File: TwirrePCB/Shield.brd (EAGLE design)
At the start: 96.2 x 53.6 mm, 60 parts, among them Q1 BSS138, Q2 BSS138, T2 BC847, U1 ARDUINO-MEGAPRO

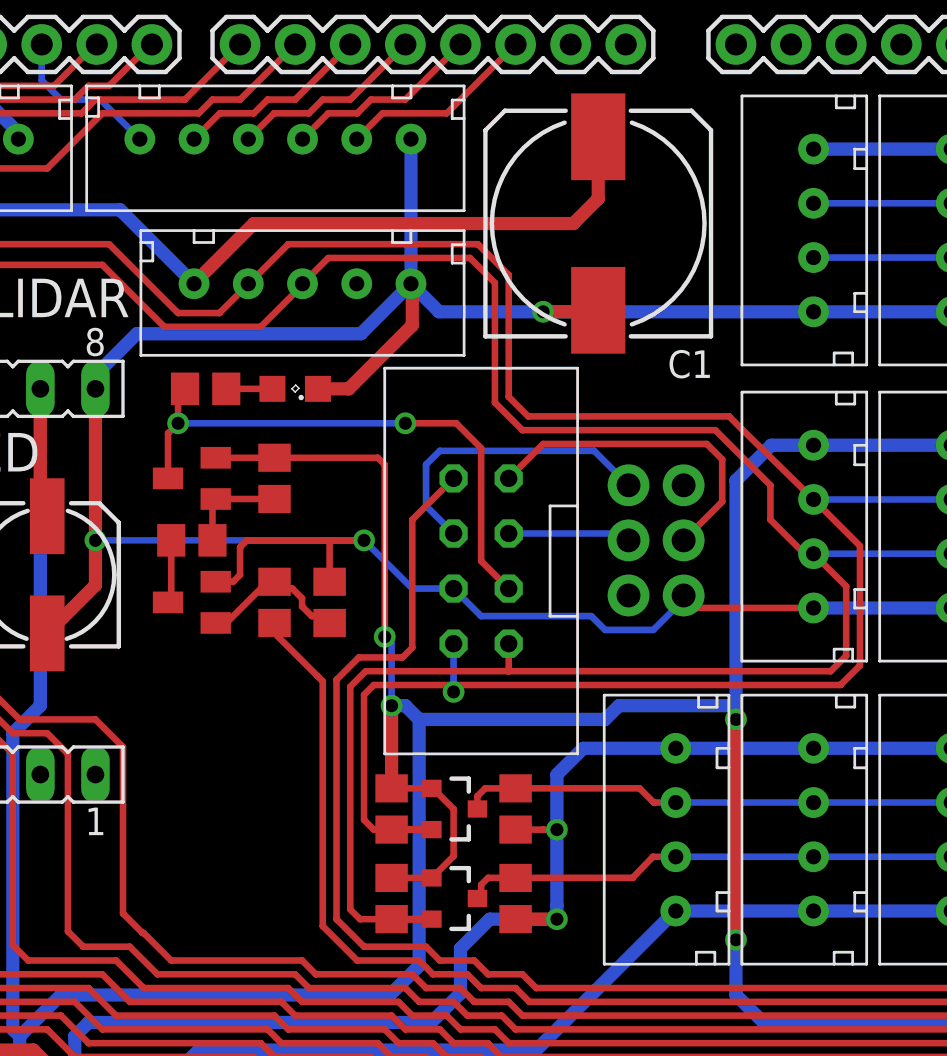
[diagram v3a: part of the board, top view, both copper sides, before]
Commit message: Minor trace modifications
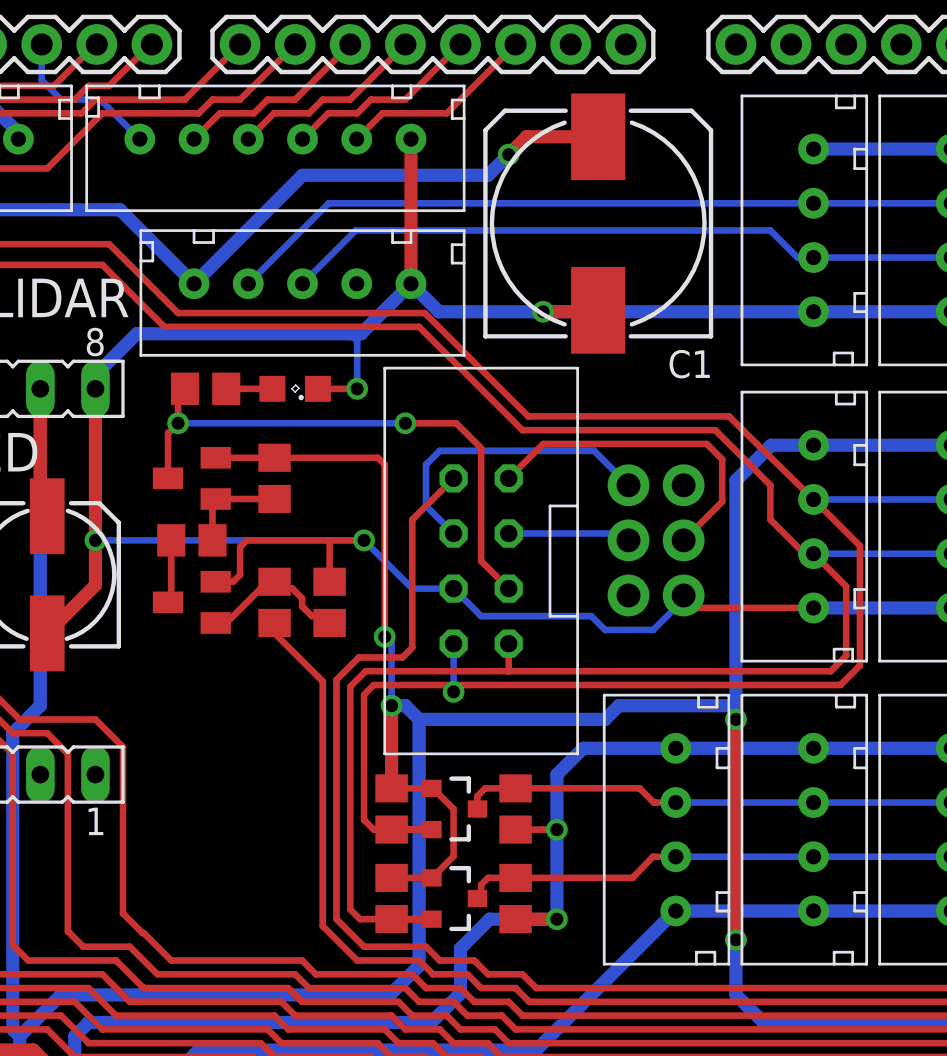
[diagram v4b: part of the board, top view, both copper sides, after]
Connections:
- net SCL_HS: now also U$12.3
- net SCL_LS: no longer U$12.3
- net SDA_HS: now also U$12.4
- net SDA_LS: no longer U$12.4
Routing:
- net SDA_HS: track 21.7 -> 49.3 mm
- net SCL_HS: track 23.7 -> 48.8 mm
- net SDA_LS: track 131.4 -> 125.5 mm
- net SCL_LS: track 135.1 -> 129.2 mm
- net GND: track 433.0 -> 430.0 mm, vias 7 -> 8
- net +5V: track 252.2 -> 250.5 mm, vias 5 -> 6
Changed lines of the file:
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@@
 <wire x1="43.46" y1="38.4775" x2="48.26" y2="38.4775" width="0.6096" layer="16"/>
 <wire x1="48.26" y1="38.4775" x2="60.725" y2="38.4775" width="0.6096" layer="16"/>
-<wire x1="37.88" y1="34.925" x2="39.300296875" y2="34.925" width="0.6096" layer="1"/>
-<wire x1="39.300296875" y1="34.925" x2="42.2275" y2="37.852203125" width="0.6096" layer="1"/>
-<wire x1="42.2275" y1="37.852203125" x2="42.2275" y2="39.4525" width="0.6096" layer="1"/>
 <contactref element="U$13" pad="1"/>
 <wire x1="1.533025" y1="21.59" x2="1.533025" y2="21.65" width="0.6096" layer="16"/>
@@
 <wire x1="17.145" y1="22.86" x2="15.875" y2="21.65" width="0.3048" layer="16"/>
 <wire x1="15.875" y1="21.65" x2="3.2575" y2="21.65" width="0.3048" layer="16"/>
-<wire x1="42.2275" y1="39.4525" x2="42.1675" y2="39.77" width="0.6096" layer="1"/>
 <contactref element="SV2" pad="8"/>
 <wire x1="27.6225" y1="34.925" x2="27.6225" y2="35.56" width="0.6096" layer="16"/>
 <wire x1="27.6225" y1="35.56" x2="29.5275" y2="37.465" width="0.6096" layer="16"/>
-<wire x1="29.5275" y1="37.465" x2="39.8625" y2="37.465" width="0.6096" layer="16"/>
+<wire x1="29.5275" y1="37.465" x2="39.37" y2="37.465" width="0.6096" layer="16"/>
+<wire x1="39.37" y1="37.465" x2="39.8625" y2="37.465" width="0.6096" layer="16"/>
 <wire x1="39.8625" y1="37.465" x2="42.1675" y2="39.77" width="0.6096" layer="16"/>
 <contactref element="U$14" pad="1"/>
@@
 <wire x1="14.986" y1="50.8" x2="14.986" y2="48.514" width="0.6096" layer="16"/>
 <wire x1="14.986" y1="48.514" x2="15.24" y2="48.26" width="0.6096" layer="16"/>
-<wire x1="42.1675" y1="39.77" x2="42.1675" y2="46.4375" width="0.6096" layer="16"/>
 <contactref element="U$25" pad="5"/>
 <wire x1="44.1325" y1="25.7175" x2="42.2275" y2="25.7175" width="0.3048" layer="16"/>
@@
 <vertex x="-1.27" y="13.0175"/>
 </polygon>
+<wire x1="37.88" y1="34.925" x2="39.6875" y2="34.925" width="0.3048" layer="1"/>
+<via x="39.6875" y="34.925" extent="1-16" drill="0.6" shape="square"/>
+<wire x1="39.6875" y1="34.925" x2="39.6875" y2="37.1475" width="0.3048" layer="16"/>
+<wire x1="39.6875" y1="37.1475" x2="39.37" y2="37.465" width="0.3048" layer="16"/>
+<wire x1="6.0325" y1="6.81" x2="6.35" y2="11.1125" width="0" layer="19" extent="16-16"/>
+<wire x1="42.1675" y1="46.4375" x2="42.1675" y2="39.77" width="0.6096" layer="1"/>
 </signal>
 <signal name="SPI_VIN">
@@
 <wire x1="62.23" y1="22.61745" x2="62.23" y2="25.82" width="0.3048" layer="1"/>
 <wire x1="62.23" y1="25.82" x2="60.725" y2="27.325" width="0.3048" layer="1"/>
-<contactref element="U$12" pad="3"/>
 <wire x1="16.8275" y1="40.64" x2="20.0025" y2="40.64" width="0.3048" layer="1"/>
 <wire x1="20.0025" y1="40.64" x2="27.94" y2="40.64" width="0.3048" layer="1"/>
 <wire x1="27.94" y1="40.64" x2="30.7975" y2="37.7825" width="0.3048" layer="1"/>
-<wire x1="30.7975" y1="37.7825" x2="35.2425" y2="37.7825" width="0.3048" layer="1"/>
-<wire x1="35.2425" y1="37.7825" x2="37.1675" y2="39.7075" width="0.3048" layer="1"/>
-<wire x1="37.1675" y1="39.7075" x2="37.1675" y2="39.77" width="0.3048" layer="1"/>
-<wire x1="37.1675" y1="39.77" x2="38.355" y2="40.9575" width="0.3048" layer="1"/>
 <contactref element="SV2" pad="5"/>
 <wire x1="20.0025" y1="34.925" x2="20.0025" y2="40.64" width="0.3048" layer="1"/>
-<wire x1="38.355" y1="40.9575" x2="44.8927375" y2="40.9575" width="0.3048" layer="1"/>
-<wire x1="44.8927375" y1="40.9575" x2="46.0375" y2="39.8127375" width="0.3048" layer="1"/>
 <wire x1="16.8275" y1="40.64" x2="7.3025" y2="50.165" width="0.3048" layer="1"/>
 <wire x1="7.3025" y1="50.165" x2="7.3025" y2="50.7365" width="0.3048" layer="1"/>
@@
 <wire x1="58.7375" y1="30.48" x2="56.1975" y2="33.02" width="0.3048" layer="1"/>
 <wire x1="56.1975" y1="33.02" x2="47.3075" y2="33.02" width="0.3048" layer="1"/>
-<wire x1="47.3075" y1="33.02" x2="46.0375" y2="34.29" width="0.3048" layer="1"/>
-<wire x1="46.0375" y1="34.29" x2="46.0375" y2="39.8127375" width="0.3048" layer="1"/>
+<wire x1="30.7975" y1="37.7825" x2="42.545" y2="37.7825" width="0.3048" layer="1"/>
+<wire x1="42.545" y1="37.7825" x2="47.3075" y2="33.02" width="0.3048" layer="1"/>
 </signal>
 <signal name="SDA_LS">
@@
 <wire x1="60.725" y1="29.825" x2="67.075" y2="29.825" width="0.3048" layer="16"/>
 <wire x1="56.8325" y1="33.655" x2="47.570525" y2="33.655" width="0.3048" layer="1"/>
-<wire x1="47.570525" y1="33.655" x2="46.6725" y2="34.553025" width="0.3048" layer="1"/>
-<wire x1="46.6725" y1="34.553025" x2="46.6725" y2="40.172596875" width="0.3048" layer="1"/>
 <wire x1="56.8325" y1="33.655" x2="57.4675" y2="33.02" width="0.3048" layer="1"/>
 <wire x1="57.4675" y1="33.02" x2="60.725" y2="29.825" width="0.3048" layer="1"/>
@@
 <wire x1="62.865" y1="22.170525" x2="62.865" y2="27.685" width="0.3048" layer="1"/>
 <wire x1="62.865" y1="27.685" x2="60.725" y2="29.825" width="0.3048" layer="1"/>
-<contactref element="U$12" pad="4"/>
 <wire x1="17.145" y1="41.5925" x2="22.5425" y2="41.5925" width="0.3048" layer="1"/>
 <wire x1="22.5425" y1="41.5925" x2="28.2575" y2="41.5925" width="0.3048" layer="1"/>
 <wire x1="28.2575" y1="41.5925" x2="31.4325" y2="38.4175" width="0.3048" layer="1"/>
-<wire x1="31.4325" y1="38.4175" x2="33.3375" y2="38.4175" width="0.3048" layer="1"/>
-<wire x1="33.3375" y1="38.4175" x2="34.6675" y2="39.7475" width="0.3048" layer="1"/>
-<wire x1="34.6675" y1="39.7475" x2="34.6675" y2="39.77" width="0.3048" layer="1"/>
-<wire x1="34.6675" y1="39.7475" x2="36.5125" y2="41.5925" width="0.3048" layer="1"/>
 <contactref element="SV2" pad="6"/>
 <wire x1="22.5425" y1="34.925" x2="22.5425" y2="41.5925" width="0.3048" layer="16"/>
 <via x="22.5425" y="41.5925" extent="1-16" drill="0.6" shape="square"/>
-<wire x1="46.6725" y1="40.172596875" x2="45.252596875" y2="41.5925" width="0.3048" layer="1"/>
-<wire x1="45.252596875" y1="41.5925" x2="36.5125" y2="41.5925" width="0.3048" layer="1"/>
 <wire x1="17.145" y1="41.5925" x2="9.8425" y2="48.895" width="0.3048" layer="1"/>
 <wire x1="9.8425" y1="48.895" x2="9.8425" y2="50.7365" width="0.3048" layer="1"/>
@@
 <via x="44.1325" y="20.955" extent="1-16" drill="0.6" shape="square"/>
 <wire x1="44.1325" y1="20.955" x2="44.1325" y2="21.2725" width="0.3048" layer="1"/>
+<wire x1="31.4325" y1="38.4175" x2="42.808025" y2="38.4175" width="0.3048" layer="1"/>
+<wire x1="42.808025" y1="38.4175" x2="47.570525" y2="33.655" width="0.3048" layer="1"/>
 </signal>
 <signal name="+5V">
@@
 <wire x1="90.805" y1="47.625" x2="90.4875" y2="47.3075" width="0.4064" layer="16"/>
 <contactref element="C1" pad="+"/>
-<wire x1="50.8" y1="46.545" x2="50.8" y2="43.6897625" width="0.6096" layer="1"/>
-<wire x1="50.8" y1="43.6897625" x2="49.6552375" y2="42.545" width="0.6096" layer="1"/>
-<wire x1="49.6552375" y1="42.545" x2="34.925" y2="42.545" width="0.6096" layer="1"/>
-<wire x1="34.925" y1="42.545" x2="32.1675" y2="39.7875" width="0.6096" layer="1"/>
-<wire x1="32.1675" y1="39.7875" x2="32.1675" y2="39.77" width="0.6096" layer="1"/>
 <wire x1="54.375" y1="18.355" x2="50.105" y2="18.355" width="0.6096" layer="16"/>
 <wire x1="50.105" y1="18.355" x2="48.895" y2="17.145" width="0.6096" layer="16"/>
 <wire x1="48.895" y1="17.145" x2="48.895" y2="14.605" width="0.6096" layer="16"/>
 <wire x1="45.7970375" y1="10.4775" x2="48.895" y2="10.4775" width="0.6096" layer="16"/>
-<wire x1="48.895" y1="11.1125" x2="48.895" y2="14.605" width="0.6096" layer="16"/>
+<wire x1="48.895" y1="10.4775" x2="48.895" y2="14.605" width="0.6096" layer="16"/>
 <wire x1="46.99" y1="10.48" x2="48.8925" y2="10.48" width="0.6096" layer="1"/>
 <wire x1="48.8925" y1="10.48" x2="48.895" y2="10.4775" width="0.6096" layer="1"/>
 <via x="48.895" y="10.4775" extent="1-16" drill="0.6" shape="square"/>
-<wire x1="48.895" y1="10.4775" x2="48.895" y2="11.1125" width="0.6096" layer="16"/>
+<wire x1="50.8" y1="46.545" x2="47.4975" y2="46.545" width="0.6096" layer="1"/>
+<wire x1="47.4975" y1="46.545" x2="46.6725" y2="45.72" width="0.6096" layer="1"/>
+<via x="46.6725" y="45.72" extent="1-16" drill="0.6" shape="square"/>
+<wire x1="46.6725" y1="45.72" x2="45.72" y2="44.7675" width="0.6096" layer="16"/>
+<wire x1="45.72" y1="44.7675" x2="37.165" y2="44.7675" width="0.6096" layer="16"/>
+<wire x1="37.165" y1="44.7675" x2="32.1675" y2="39.77" width="0.6096" layer="16"/>
 </signal>
 <signal name="SDA_LS_5">
@@
 <wire x1="73.9775" y1="47.3075" x2="73.9775" y2="49.2125" width="0.3048" layer="16"/>
 <wire x1="73.9775" y1="49.2125" x2="72.39" y2="50.8" width="0.3048" layer="16"/>
+<contactref element="U$12" pad="4"/>
+<wire x1="60.725" y1="43.4775" x2="38.375" y2="43.4775" width="0.3048" layer="16"/>
+<wire x1="38.375" y1="43.4775" x2="34.6675" y2="39.77" width="0.3048" layer="16"/>
 </signal>
 <signal name="SCL_HS">
@@
 <wire x1="75.565" y1="46.6725" x2="74.93" y2="47.3075" width="0.3048" layer="16"/>
 <wire x1="74.93" y1="47.3075" x2="74.93" y2="50.8" width="0.3048" layer="16"/>
+<contactref element="U$12" pad="3"/>
+<wire x1="60.725" y1="40.9775" x2="59.9875" y2="40.9775" width="0.3048" layer="16"/>
+<wire x1="59.9875" y1="40.9775" x2="58.7375" y2="42.2275" width="0.3048" layer="16"/>
+<wire x1="58.7375" y1="42.2275" x2="39.625" y2="42.2275" width="0.3048" layer="16"/>
+<wire x1="39.625" y1="42.2275" x2="37.1675" y2="39.77" width="0.3048" layer="16"/>
 </signal>
 <signal name="N$7">

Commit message: Increase LED Resistor values
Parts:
- R20, R21, R6, R7: value 100 -> 220
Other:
- board text added: "FLIR"
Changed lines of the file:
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@@
 <grid distance="0.0125" unitdist="inch" unit="inch" style="lines" multiple="1" display="no" altdistance="0.025" altunitdist="inch" altunit="inch"/>
 <layers>
-<layer number="1" name="Top" color="4" fill="1" visible="yes" active="yes"/>
-<layer number="16" name="Bottom" color="1" fill="1" visible="yes" active="yes"/>
+<layer number="1" name="Top" color="4" fill="1" visible="no" active="yes"/>
+<layer number="16" name="Bottom" color="1" fill="1" visible="no" active="yes"/>
 <layer number="17" name="Pads" color="2" fill="1" visible="yes" active="yes"/>
 <layer number="18" name="Vias" color="2" fill="1" visible="yes" active="yes"/>
@@
 <dimension x1="-1.27" y1="53.33" x2="94.92" y2="53.33" x3="46.825" y3="59.3725" textsize="1.778" layer="37"/>
 <dimension x1="94.92" y1="53.33" x2="94.92" y2="-0.3175" x3="100.6475" y3="26.50625" textsize="1.778" layer="37"/>
+<text x="34.29" y="19.05" size="1.9304" layer="25">FLIR</text>
 </plain>
 <attributes>
@@
 <attribute name="VALUE" x="14.605" y="33.02" size="1.27" layer="27" rot="R180"/>
 </element>
-<element name="R20" library="resistor" package="R0805" value="100" x="8.89" y="42.2275" smashed="yes">
+<element name="R20" library="resistor" package="R0805" value="220" x="8.89" y="42.2275" smashed="yes">
 <attribute name="VALUE" x="8.255" y="39.6875" size="1.27" layer="27"/>
 </element>
-<element name="R6" library="resistor" package="R0805" value="100" x="8.89" y="40.005" smashed="yes">
+<element name="R6" library="resistor" package="R0805" value="220" x="8.89" y="40.005" smashed="yes">
 <attribute name="VALUE" x="8.255" y="37.465" size="1.27" layer="27"/>
 </element>
-<element name="R7" library="resistor" package="R0805" value="100" x="8.89" y="37.7825" smashed="yes">
+<element name="R7" library="resistor" package="R0805" value="220" x="8.89" y="37.7825" smashed="yes">
 <attribute name="VALUE" x="8.255" y="35.2425" size="1.27" layer="27"/>
 </element>
@@
 <element name="U$14" library="Arduino-Boards" package="JST-3" value="JST-3" x="89.8525" y="22.5425" rot="R90"/>
 <element name="U$15" library="Arduino-Boards" package="JST-3" value="JST-3" x="89.8525" y="12.065" rot="R90"/>
-<element name="R21" library="resistor" package="R0805" value="100" x="89.8525" y="51.1175" smashed="yes">
+<element name="R21" library="resistor" package="R0805" value="220" x="89.8525" y="51.1175" smashed="yes">
 <attribute name="VALUE" x="89.2175" y="48.5775" size="1.27" layer="27"/>
 </element>
@@
 <wire x1="39.6875" y1="34.925" x2="39.6875" y2="37.1475" width="0.3048" layer="16"/>
 <wire x1="39.6875" y1="37.1475" x2="39.37" y2="37.465" width="0.3048" layer="16"/>
-<wire x1="6.0325" y1="6.81" x2="6.35" y2="11.1125" width="0" layer="19" extent="16-16"/>
 <wire x1="42.1675" y1="46.4375" x2="42.1675" y2="39.77" width="0.6096" layer="1"/>
 </signal>
